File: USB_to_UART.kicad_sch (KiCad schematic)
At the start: 38 parts, among them U30 M93C46-WDW6TP, U31 FT4232HQ, Y2 12MHz

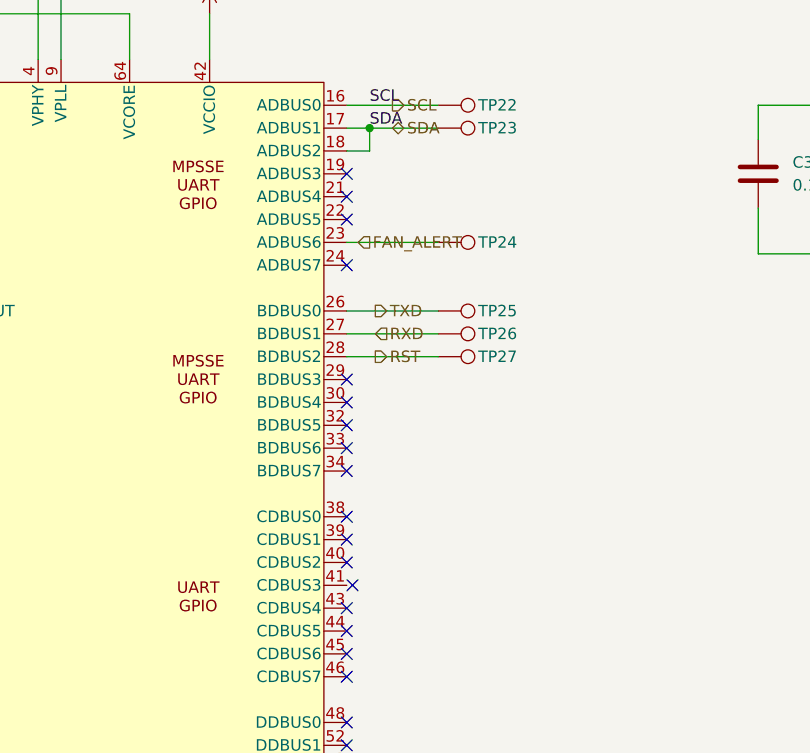
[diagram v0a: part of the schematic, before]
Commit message: board stakup updated and schematic is updated
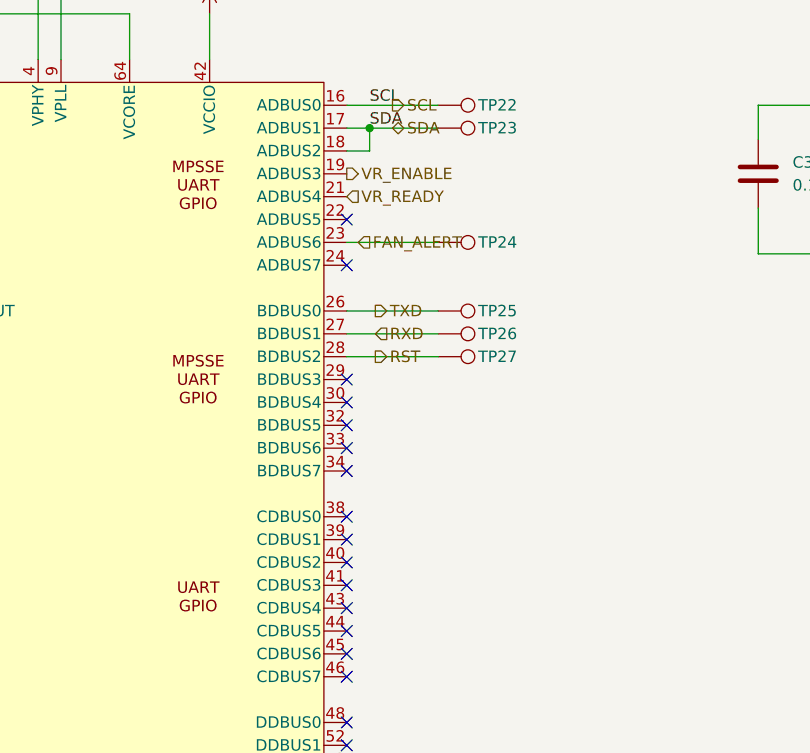
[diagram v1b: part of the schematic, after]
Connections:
- net VR_ENABLE: now reaches U31.19 (ADBUS3)
- net VR_READY: now reaches U31.21 (ADBUS4)
- no-connect marks 27 -> 25
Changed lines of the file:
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@@
 	)
 	(no_connect
-		(at 208.915 119.38)
+		(at 208.915 129.54)
 	)
 	(no_connect
@@
 	)
 	(no_connect
+		(at 208.915 124.46)
+	)
+	(no_connect
 		(at 208.915 172.72)
 	)
@@
 	)
 	(no_connect
-		(at 209.55 165.1)
+		(at 208.915 165.1)
 	)
 	(no_connect
@@
 	)
 	(no_connect
-		(at 208.915 121.92)
-	)
-	(no_connect
 		(at 208.915 190.5)
 	)
@@
 	(no_connect
 		(at 208.915 182.88)
-	)
-	(no_connect
-		(at 208.915 124.46)
-	)
-	(no_connect
-		(at 208.915 129.54)
 	)
 	(no_connect
@@
 		)
 	)
+	(hierarchical_label "VR_READY"
+		(shape input)
+		(at 208.915 121.92 0)
+		(effects
+			(font
+				(size 1.27 1.27)
+			)
+			(justify left)
+		)
+	)
+	(hierarchical_label "VR_ENABLE"
+		(shape output)
+		(at 208.915 119.38 0)
+		(effects
+			(font
+				(size 1.27 1.27)
+			)
+			(justify left)
+		)
+	)

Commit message: updated schematic working on layout
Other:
- company: (none) -> Author: Aadhi M
- title: (none) -> PC-AXE
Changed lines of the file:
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@@
 	(generator_version "9.0")
 	(paper "A3")
+	(title_block
+		(title "PC-AXE")
+		(company "Author: Aadhi M")
+	)
 	(junction
 		(at 153.035 134.62)

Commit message: Updated new layout and routing of PCB
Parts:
- added TP28, TP29: TestPoint, TestPoint:TestPoint_Pad_D1.5mm, symbol Connector:TestPoint
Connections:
- net DN: now also TP28.1
- net DP: now also TP29.1
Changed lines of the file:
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@@
 	)
 	(junction
+		(at 158.75 152.4)
+		(diameter 0)
+		(color 0 0 0 0)
+	)
+	(junction
 		(at 135.255 205.74)
 		(diameter 0)
@@
 	)
 	(junction
+		(at 158.115 149.86)
+		(diameter 0)
+		(color 0 0 0 0)
+	)
+	(junction
 		(at 142.875 93.98)
 		(diameter 0)
@@
 	(wire
 		(pts
+			(xy 147.955 153.67) (xy 158.75 153.67)
+		)
+		(stroke
+			(width 0)
+			(type default)
+		)
+	)
+	(wire
+		(pts
 			(xy 99.695 78.74) (xy 99.695 81.28)
 		)
@@
 	(wire
 		(pts
-			(xy 157.48 152.4) (xy 160.655 152.4)
+			(xy 157.48 152.4) (xy 158.75 152.4)
+		)
+		(stroke
+			(width 0)
+			(type default)
+		)
+	)
+	(wire
+		(pts
+			(xy 158.75 153.67) (xy 158.75 152.4)
 		)
 		(stroke
@@
 	(wire
 		(pts
+			(xy 137.16 148.59) (xy 137.16 149.86)
+		)
+		(stroke
+			(width 0)
+			(type default)
+		)
+	)
+	(wire
+		(pts
 			(xy 211.455 114.3) (xy 219.075 114.3)
 		)
@@
 	(wire
 		(pts
+			(xy 158.115 149.86) (xy 160.655 149.86)
+		)
+		(stroke
+			(width 0)
+			(type default)
+		)
+	)
+	(wire
+		(pts
 			(xy 174.625 81.28) (xy 174.625 106.68)
 		)
@@
 	(wire
 		(pts
+			(xy 158.115 149.86) (xy 158.115 148.59)
+		)
+		(stroke
+			(width 0)
+			(type default)
+		)
+	)
+	(wire
+		(pts
 			(xy 137.795 167.64) (xy 146.685 167.64)
 		)
@@
 	(wire
 		(pts
+			(xy 158.115 148.59) (xy 137.16 148.59)
+		)
+		(stroke
+			(width 0)
+			(type default)
+		)
+	)
+	(wire
+		(pts
 			(xy 61.595 177.8) (xy 61.595 213.36)
 		)
@@
 	(wire
 		(pts
+			(xy 158.75 152.4) (xy 160.655 152.4)
+		)
+		(stroke
+			(width 0)
+			(type default)
+		)
+	)
+	(wire
+		(pts
 			(xy 294.005 111.76) (xy 306.705 111.76)
 		)
@@
 	(wire
 		(pts
-			(xy 157.48 149.86) (xy 160.655 149.86)
+			(xy 157.48 149.86) (xy 158.115 149.86)
 		)
 		(stroke
@@
 	(wire
 		(pts
+			(xy 147.955 152.4) (xy 147.955 153.67)
+		)
+		(stroke
+			(width 0)
+			(type default)
+		)
+	)
+	(wire
+		(pts
 			(xy 73.025 210.82) (xy 79.375 210.82)
 		)
@@
 	(symbol
 		(lib_id "Connector:TestPoint")
+		(at 147.955 152.4 90)
+		(unit 1)
+		(exclude_from_sim no)
+		(in_bom no)
+		(on_board yes)
+		(dnp no)
+		(property "Reference" "TP29"
+			(at 143.51 152.4 90)
+			(effects
+				(font
+					(size 1.27 1.27)
+				)
+				(justify left)
+			)
+		)
+		(property "Value" "TestPoint"
+			(at 147.2692 150.9268 0)
+			(effects
+				(font
+					(size 1.27 1.27)
+				)
+				(justify left)
+				(hide yes)
+			)
+		)
+		(property "Footprint" "TestPoint:TestPoint_Pad_D1.5mm"
+			(at 147.955 147.32 0)
+			(effects
+				(font
+					(size 1.27 1.27)
+				)
+				(hide yes)
+			)
+		)
+		(property "Datasheet" ""
+			(at 147.955 147.32 0)
+			(effects
+				(font
+					(size 1.27 1.27)
+				)
+				(hide yes)
+			)
+		)
+		(property "Description" ""
+			(at 147.955 152.4 0)
+			(effects
+				(font
+					(size 1.27 1.27)
+				)
+				(hide yes)
+			)
+		)
+		(pin "1"
+		)
+		(instances
+			(project "PC-AXE"
+				(path "/540dc3bd-590a-41f0-90cd-0aeeeb4ef5ba/6a91f013-747b-4e59-9f69-797c0dae88cc"
+					(reference "TP29")
+					(unit 1)
+				)
+			)
+		)
+	)
+	(symbol
+		(lib_id "Connector:TestPoint")
 		(at 130.175 163.83 90)
 		(unit 1)
@@
 					(unit 1)
 				)
+			)
+		)
+	)
+	(symbol
+		(lib_id "Connector:TestPoint")
+		(at 137.16 149.86 90)
+		(unit 1)
+		(exclude_from_sim no)
+		(in_bom no)
+		(on_board yes)
+		(dnp no)
+		(property "Reference" "TP28"
+			(at 132.715 149.86 90)
+			(effects
+				(font
+					(size 1.27 1.27)
+				)
+				(justify left)
+			)
+		)
+		(property "Value" "TestPoint"
+			(at 136.4742 148.3868 0)
+			(effects
+				(font
+					(size 1.27 1.27)
+				)
+				(justify left)
+				(hide yes)
+			)
+		)
+		(property "Footprint" "TestPoint:TestPoint_Pad_D1.5mm"
+			(at 137.16 144.78 0)
+			(effects
+				(font
+					(size 1.27 1.27)
+				)
+				(hide yes)
+			)
+		)
+		(property "Datasheet" ""
+			(at 137.16 144.78 0)
+			(effects
+				(font
+					(size 1.27 1.27)
+				)
+				(hide yes)
+			)
+		)
+		(property "Description" ""
+			(at 137.16 149.86 0)
+			(effects
+				(font
+					(size 1.27 1.27)
+				)
+				(hide yes)
+			)
+		)
+		(pin "1"
+		)
+		(instances
+			(project "PC-AXE"
+				(path "/540dc3bd-590a-41f0-90cd-0aeeeb4ef5ba/6a91f013-747b-4e59-9f69-797c0dae88cc"
+					(reference "TP28")
+					(unit 1)
+				)

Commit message: Updated after DRC
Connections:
- net LDO_EN: now reaches U31.24 (ADBUS7)
- no-connect marks 25 -> 24
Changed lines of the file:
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@@
-	)
-	(no_connect
-		(at 208.915 129.54)
 	)
 	(no_connect
@@
 		(effects
 			(font
+				(size 1.27 1.27)
+			)
+			(justify left)
+		)
+	)
+	(hierarchical_label "LDO_EN"
+		(shape output)
+		(at 208.915 129.54 0)
+		(effects
+			(font
